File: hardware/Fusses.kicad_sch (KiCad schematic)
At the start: 0 parts

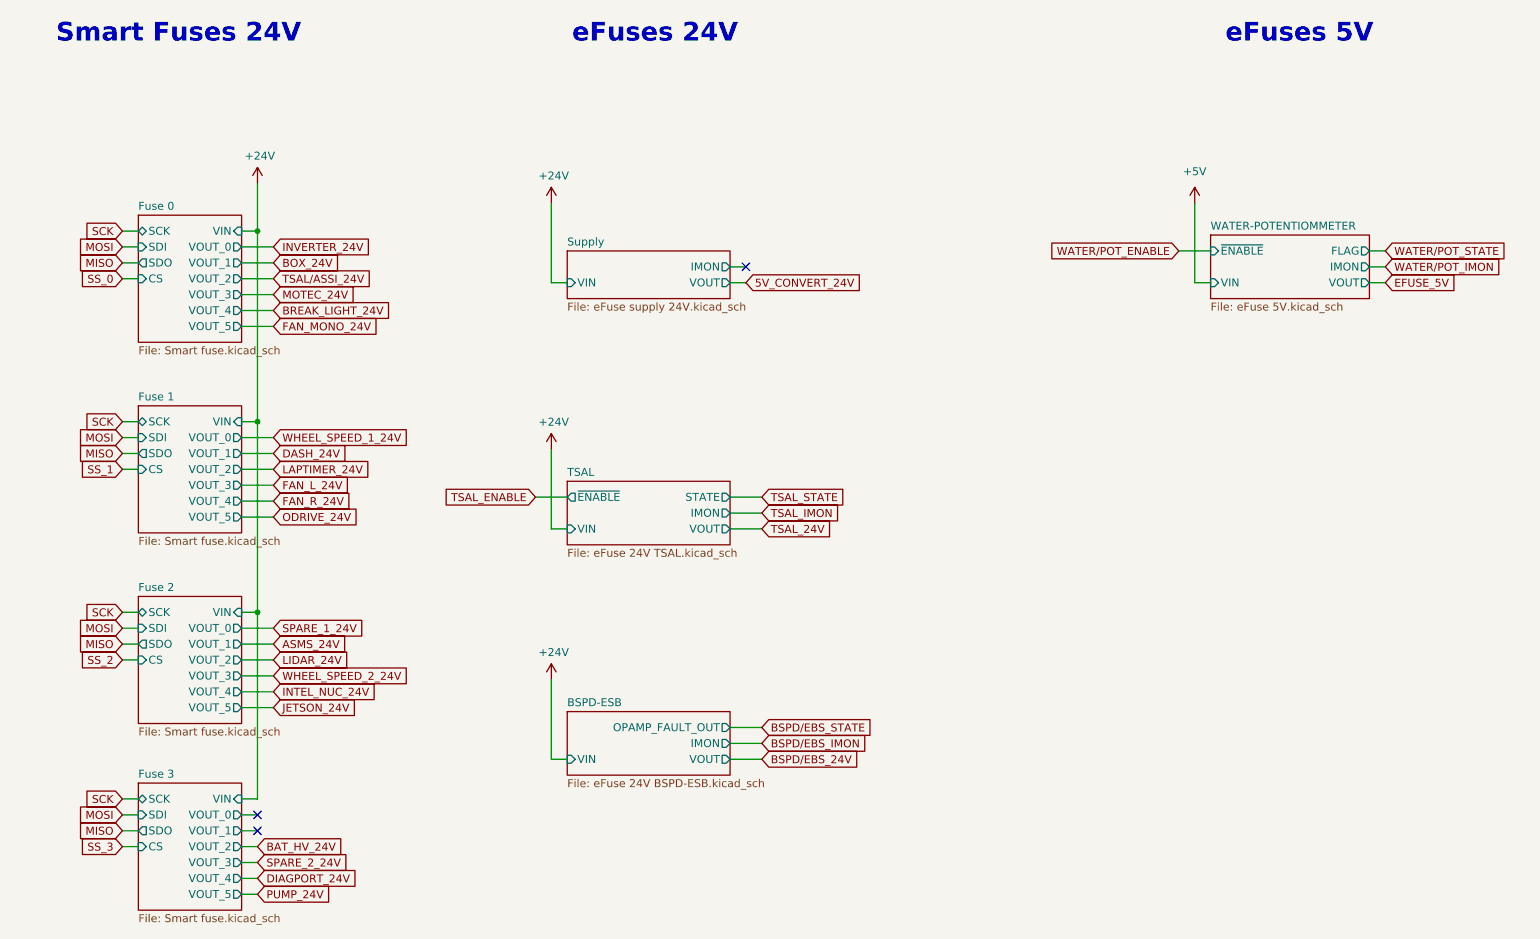
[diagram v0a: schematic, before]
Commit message: debuged the board, changed one opto for mosfet, changed the way water and potentiometers were supplied. Also standrised opamps (yoinked opamps from data Data_Acquisition_Cards)
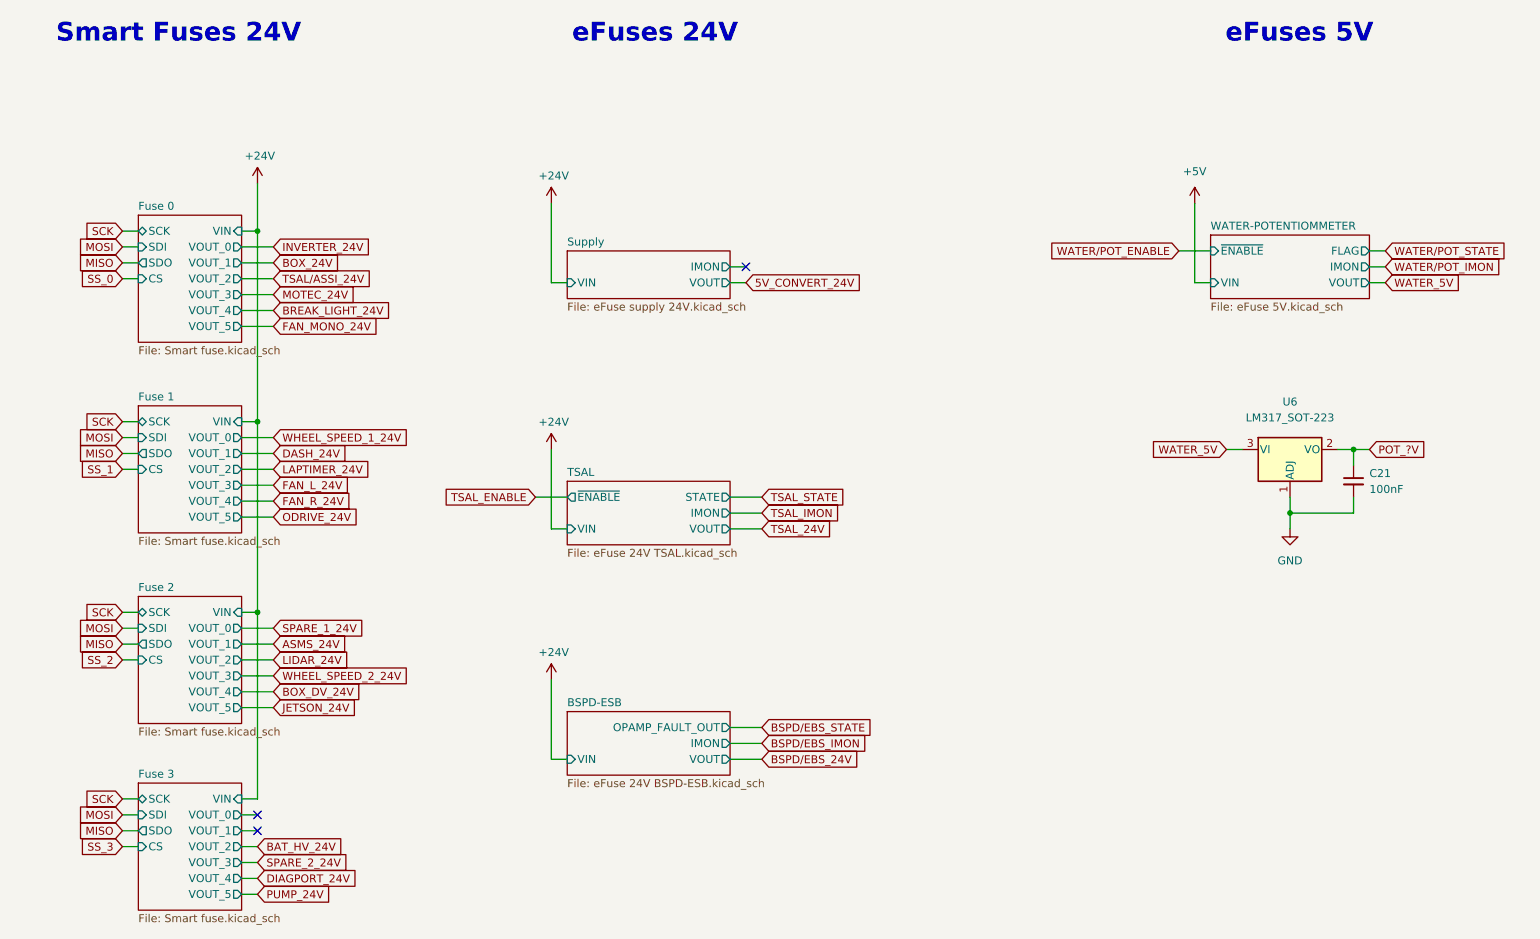
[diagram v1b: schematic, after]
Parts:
- added C21: 100nF, Capacitor_SMD:C_0603_1608Metric, symbol Device:C_Small
- added U6: LM317_SOT-223, Package_TO_SOT_SMD:SOT-223-3_TabPin2, symbol Regulator_Linear:LM317_SOT-223
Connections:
- new net GND: C21.2, U6.1 (ADJ)
- new net POT_?V: C21.1, U6.2 (VO)
- new net WATER_5V: U6.3 (VI)
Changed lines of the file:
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@@
   (junction (at 66.04 93.345) (diameter 0) (color 0 0 0 0)
+  )
+  (junction (at 241.3 97.79) (diameter 0) (color 0 0 0 0)
+  )
+  (junction (at 231.14 107.95) (diameter 0) (color 0 0 0 0)
   )
   (junction (at 66.04 123.825) (diameter 0) (color 0 0 0 0)
@@
     (stroke (width 0) (type default) (color 0 0 0 0))
   )
+  (wire (pts (xy 231.14 107.95) (xy 241.3 107.95))
+    (stroke (width 0) (type default) (color 0 0 0 0))
+  )
   (wire (pts (xy 63.5 133.985) (xy 68.58 133.985))
     (stroke (width 0) (type default) (color 0 0 0 0))
@@
     (stroke (width 0) (type default) (color 0 0 0 0))
   )
+  (wire (pts (xy 231.14 107.95) (xy 231.14 110.49))
+    (stroke (width 0) (type default) (color 0 0 0 0))
+  )
   (wire (pts (xy 66.04 161.29) (xy 63.5 161.29))
     (stroke (width 0) (type default) (color 0 0 0 0))
@@
     (stroke (width 0) (type default) (color 0 0 0 0))
   )
+  (wire (pts (xy 241.3 97.79) (xy 243.84 97.79))
+    (stroke (width 0) (type default) (color 0 0 0 0))
+  )
   (wire (pts (xy 44.45 67.945) (xy 46.99 67.945))
     (stroke (width 0) (type default) (color 0 0 0 0))
@@
     (stroke (width 0) (type default) (color 0 0 0 0))
   )
+  (wire (pts (xy 223.52 97.79) (xy 220.98 97.79))
+    (stroke (width 0) (type default) (color 0 0 0 0))
+  )
   (wire (pts (xy 141.605 105.41) (xy 146.685 105.41))
     (stroke (width 0) (type default) (color 0 0 0 0))
   )
+  (wire (pts (xy 241.3 97.79) (xy 241.3 100.33))
+    (stroke (width 0) (type default) (color 0 0 0 0))
+  )
   (wire (pts (xy 243.84 66.04) (xy 246.38 66.04))
     (stroke (width 0) (type default) (color 0 0 0 0))
@@
     (stroke (width 0) (type default) (color 0 0 0 0))
   )
+  (wire (pts (xy 241.3 105.41) (xy 241.3 107.95))
+    (stroke (width 0) (type default) (color 0 0 0 0))
+  )
   (wire (pts (xy 68.58 95.885) (xy 63.5 95.885))
     (stroke (width 0) (type default) (color 0 0 0 0))
@@
     (stroke (width 0) (type default) (color 0 0 0 0))
   )
+  (wire (pts (xy 238.76 97.79) (xy 241.3 97.79))
+    (stroke (width 0) (type default) (color 0 0 0 0))
+  )
   (wire (pts (xy 63.5 73.025) (xy 68.58 73.025))
     (stroke (width 0) (type default) (color 0 0 0 0))
@@
   )
   (wire (pts (xy 63.5 126.365) (xy 68.58 126.365))
+    (stroke (width 0) (type default) (color 0 0 0 0))
+  )
+  (wire (pts (xy 231.14 105.41) (xy 231.14 107.95))
     (stroke (width 0) (type default) (color 0 0 0 0))
   )
@@
     )
   )
-  (global_label "EFUSE_5V" (shape input) (at 246.38 71.12 0) (fields_autoplaced)
+  (global_label "WATER_5V" (shape input) (at 246.38 71.12 0) (fields_autoplaced)
     (effects (font (size 1.27 1.27)) (justify left))
     (property "Intersheet References" "${INTERSHEET_REFS}" (id 0) (at 257.8966 71.0406 0)
@@
     )
   )
-  (global_label "INTEL_NUC_24V" (shape input) (at 68.58 136.525 0) (fields_autoplaced)
-    (effects (font (size 1.27 1.27)) (justify left))
-    (property "Intersheet References" "${INTERSHEET_REFS}" (id 0) (at 85.358 136.4456 0)
+  (global_label "BOX_DV_24V" (shape input) (at 68.58 136.525 0) (fields_autoplaced)
+    (effects (font (size 1.27 1.27)) (justify left))
+    (property "Intersheet References" "${INTERSHEET_REFS}" (id 0) (at 82.5156 136.4456 0)
       (effects (font (size 1.27 1.27)) (justify left) hide)
     )
@@
     )
   )
+  (global_label "WATER_5V" (shape input) (at 220.98 97.79 180) (fields_autoplaced)
+    (effects (font (size 1.27 1.27)) (justify right))
+    (property "Intersheet References" "${INTERSHEET_REFS}" (id 0) (at 209.4634 97.8694 0)
+      (effects (font (size 1.27 1.27)) (justify right) hide)
+    )
+  )
   (global_label "PUMP_24V" (shape input) (at 66.04 168.91 0) (fields_autoplaced)
     (effects (font (size 1.27 1.27)) (justify left))
@@
     (effects (font (size 1.27 1.27)) (justify left))
     (property "Intersheet References" "${INTERSHEET_REFS}" (id 0) (at 83.5437 126.2856 0)
+      (effects (font (size 1.27 1.27)) (justify left) hide)
+    )
+  )
+  (global_label "POT_?V" (shape input) (at 243.84 97.79 0) (fields_autoplaced)
+    (effects (font (size 1.27 1.27)) (justify left))
+    (property "Intersheet References" "${INTERSHEET_REFS}" (id 0) (at 252.8771 97.7106 0)
       (effects (font (size 1.27 1.27)) (justify left) hide)
     )
@@
       (effects (font (size 1.27 1.27)) hide)
     )
+  )
+  (symbol (lib_id "Regulator_Linear:LM317_SOT-223") (at 231.14 97.79 0) (unit 1)
+    (in_bom yes) (on_board yes) (fields_autoplaced)
+    (property "Reference" "U6" (id 0) (at 231.14 90.17 0))
+    (property "Value" "LM317_SOT-223" (id 1) (at 231.14 92.71 0))
+    (property "Footprint" "Package_TO_SOT_SMD:SOT-223-3_TabPin2" (id 2) (at 231.14 91.44 0)
+      (effects (font (size 1.27 1.27) italic) hide)
+    )
+    (property "Datasheet" "http://www.ti.com/lit/ds/symlink/lm317.pdf" (id 3) (at 231.14 97.79 0)
+      (effects (font (size 1.27 1.27)) hide)
+    )
+    (pin "1")
+    (pin "2")
+    (pin "3")
   )
   (symbol (lib_id "power:+24V") (at 66.04 55.245 0) (unit 1)
@@
     (pin "1")
   )
+  (symbol (lib_id "Device:C_Small") (at 241.3 102.87 0) (unit 1)
+    (in_bom yes) (on_board yes) (fields_autoplaced)
+    (property "Reference" "C21" (id 0) (at 243.84 101.6062 0)
+      (effects (font (size 1.27 1.27)) (justify left))
+    )
+    (property "Value" "100nF" (id 1) (at 243.84 104.1462 0)
+      (effects (font (size 1.27 1.27)) (justify left))
+    )
+    (property "Footprint" "Capacitor_SMD:C_0603_1608Metric" (id 2) (at 241.3 102.87 0)
+      (effects (font (size 1.27 1.27)) hide)
+    )
+    (property "Datasheet" "~" (id 3) (at 241.3 102.87 0)
+      (effects (font (size 1.27 1.27)) hide)
+    )
+    (pin "1")
+    (pin "2")
+  )
   (symbol (lib_id "power:+5V") (at 215.9 58.42 0) (unit 1)
     (in_bom yes) (on_board yes)
@@
       (effects (font (size 1.27 1.27)) hide)
     )
+    (pin "1")
+  )
+  (symbol (lib_id "power:GND") (at 231.14 110.49 0) (mirror y) (unit 1)
+    (in_bom yes) (on_board yes) (fields_autoplaced)
+    (property "Reference" "#PWR0154" (id 0) (at 231.14 116.84 0)
+      (effects (font (size 1.27 1.27)) hide)
+    )
+    (property "Value" "GND" (id 1) (at 231.14 115.57 0))
+    (property "Footprint" "" (id 2) (at 231.14 110.49 0)
+      (effects (font (size 1.27 1.27)) hide)
+    )
+    (property "Datasheet" "" (id 3) (at 231.14 110.49 0)
+      (effects (font (size 1.27 1.27)) hide)
+    )

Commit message: currected TSAL, cause it can't be controled via external logic
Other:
- sheet TSAL: file eFuse 24V TSAL.kicad_sch -> eFuse 24V BSPD-ESB.kicad_sch
- sheet TSAL ports: added OPAMP_FAULT_OUT; removed STATE, ~{ENABLE}
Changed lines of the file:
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@@
-    (stroke (width 0) (type default) (color 0 0 0 0))
-  )
-  (wire (pts (xy 115.57 105.41) (xy 110.49 105.41))
     (stroke (width 0) (type default) (color 0 0 0 0))
   )
@@
     (effects (font (size 1.27 1.27)) (justify right))
     (property "Intersheet References" "${INTERSHEET_REFS}" (id 0) (at 192.2277 65.9606 0)
-      (effects (font (size 1.27 1.27)) (justify right) hide)
-    )
-  )
-  (global_label "TSAL_ENABLE" (shape input) (at 110.49 105.41 180) (fields_autoplaced)
-    (effects (font (size 1.27 1.27)) (justify right))
-    (property "Intersheet References" "${INTERSHEET_REFS}" (id 0) (at 95.8891 105.3306 0)
       (effects (font (size 1.27 1.27)) (justify right) hide)
     )
@@
     (pin "1")
   )
+  (sheet (at 115.57 102.87) (size 26.035 10.16) (fields_autoplaced)
+    (stroke (width 0.1524) (type solid) (color 0 0 0 0))
+    (fill (color 0 0 0 0.0000))
+    (property "Sheet name" "TSAL" (id 0) (at 115.57 102.1584 0)
+      (effects (font (size 1.27 1.27)) (justify left bottom))
+    )
+    (property "Sheet file" "eFuse 24V BSPD-ESB.kicad_sch" (id 1) (at 115.57 113.6146 0)
+      (effects (font (size 1.27 1.27)) (justify left top))
+    )
+    (pin "OPAMP_FAULT_OUT" output (at 141.605 105.41 0)
+      (effects (font (size 1.27 1.27)) (justify right))
+    )
+    (pin "VIN" input (at 115.57 110.49 180)
+      (effects (font (size 1.27 1.27)) (justify left))
+    )
+    (pin "VOUT" output (at 141.605 110.49 0)
+      (effects (font (size 1.27 1.27)) (justify right))
+    )
+    (pin "IMON" output (at 141.605 107.95 0)
+      (effects (font (size 1.27 1.27)) (justify right))
+    )
+  )
   (sheet (at 46.99 121.285) (size 16.51 20.32) (fields_autoplaced)
     (stroke (width 0) (type solid) (color 0 0 0 0))
@@
       (effects (font (size 1.27 1.27)) (justify right))
     )
-  )
-  (sheet (at 115.57 102.87) (size 26.035 10.16) (fields_autoplaced)
-    (stroke (width 0.1524) (type solid) (color 0 0 0 0))
-    (fill (color 0 0 0 0.0000))
-    (property "Sheet name" "TSAL" (id 0) (at 115.57 102.1584 0)
-      (effects (font (size 1.27 1.27)) (justify left bottom))
-    )
-    (property "Sheet file" "eFuse 24V TSAL.kicad_sch" (id 1) (at 115.57 113.6146 0)
-      (effects (font (size 1.27 1.27)) (justify left top))
-    )
-    (pin "VIN" input (at 115.57 110.49 180)
-      (effects (font (size 1.27 1.27)) (justify left))
-    )
-    (pin "VOUT" output (at 141.605 110.49 0)
-      (effects (font (size 1.27 1.27)) (justify right))
-    )
-    (pin "IMON" output (at 141.605 107.95 0)
-      (effects (font (size 1.27 1.27)) (justify right))
-    )
-    (pin "~{ENABLE}" output (at 115.57 105.41 180)
-      (effects (font (size 1.27 1.27)) (justify left))
-    )
-    (pin "STATE" output (at 141.605 105.41 0)
-      (effects (font (size 1.27 1.27)) (justify right))
-    )

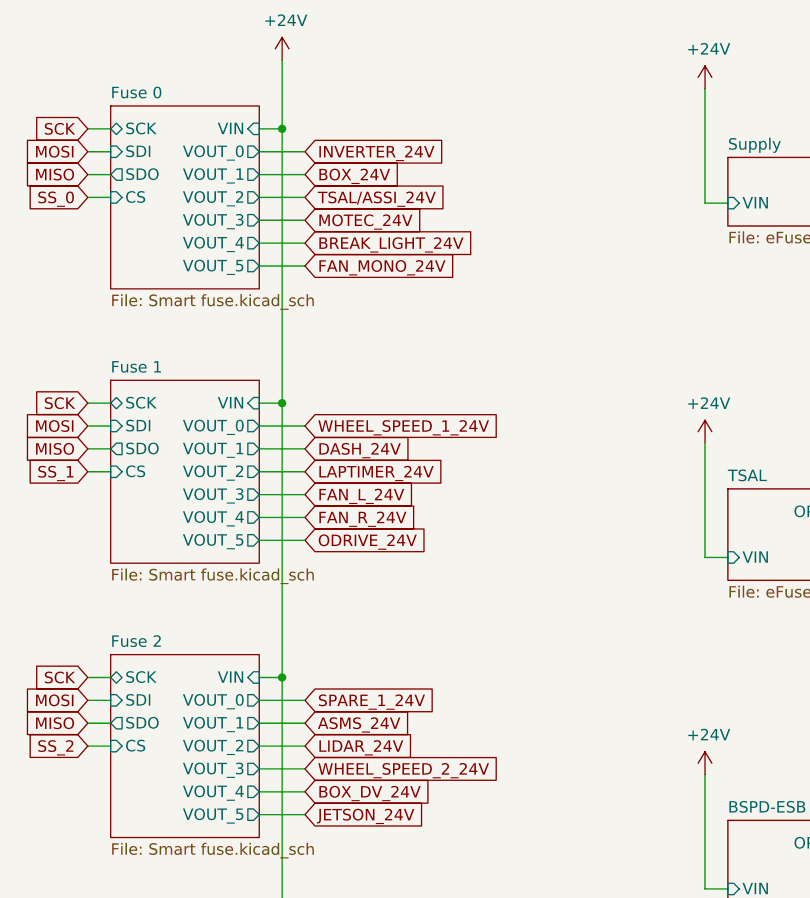
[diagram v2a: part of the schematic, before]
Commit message: nameing scheme update
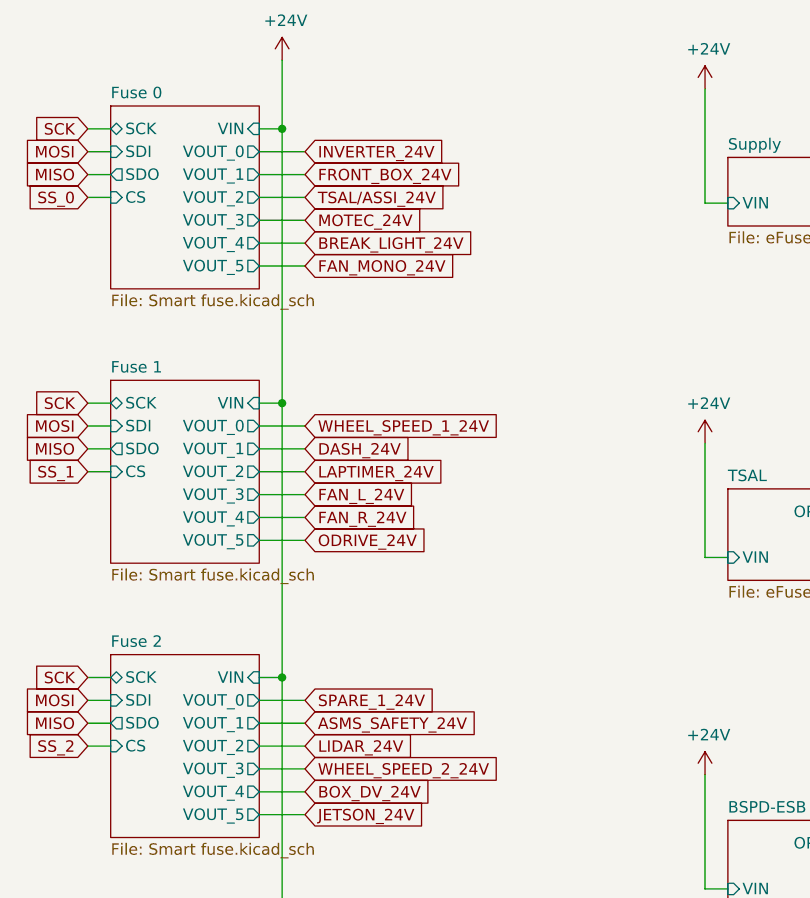
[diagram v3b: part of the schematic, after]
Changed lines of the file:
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@@
     )
   )
-  (global_label "ASMS_24V" (shape input) (at 68.58 128.905 0) (fields_autoplaced)
+  (global_label "ASMS_SAFETY_24V" (shape input) (at 68.58 128.905 0) (fields_autoplaced)
     (effects (font (size 1.27 1.27)) (justify left))
-    (property "Intersheet References" "${INTERSHEET_REFS}" (id 0) (at 80.3385 128.8256 0)
+    (property "Intersheet References" "${INTERSHEET_REFS}" (id 0) (at 87.898 128.8256 0)
       (effects (font (size 1.27 1.27)) (justify left) hide)
     )
@@
     )
   )
-  (global_label "BOX_24V" (shape input) (at 68.58 67.945 0) (fields_autoplaced)
+  (global_label "FRONT_BOX_24V" (shape input) (at 68.58 67.945 0) (fields_autoplaced)
     (effects (font (size 1.27 1.27)) (justify left))
-    (property "Intersheet References" "${INTERSHEET_REFS}" (id 0) (at 79.1894 67.8656 0)
+    (property "Intersheet References" "${INTERSHEET_REFS}" (id 0) (at 86.1442 67.8656 0)
       (effects (font (size 1.27 1.27)) (justify left) hide)
     )
